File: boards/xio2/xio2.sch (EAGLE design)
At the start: 268 parts, among them J1 12401598E4#2A, Q1 BSS138, Q2 BSS138, X1 MINI-USB-UX60-MB-5ST, Y2 NX3225SA-12.000MHZ-STD-CSR-1

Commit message: More work on the S7. The parallel bus is now alive
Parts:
- added MUX-HI, MUX-LO: IDTQS3VH257, sjg-logic:IDTQS3VH257
- renumbered U$1 to S7
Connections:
- new net HOST_!EXTSEL!: JP1.35, S7-B14.IO_L17P_T2_D30_14@J11
- new net HOST_!HALT!: JP1.37, S7-B14.IO_L17N_T2_D29_14@J12
- new net HOST_!IRQ!: JP1.39, S7-B14.IO_L19P_T3_D26_14@K11
- new net HOST_!MPD!: JP1.32, S7-B14.IO_L19N_T3_D25_VREF_14@K12
- new net HOST_!REF!: JP1.34, S7-B14.IO_L20P_T3_D24_14@M11
- new net HOST_!RST!: JP1.36, S7-B14.IO_L20N_T3_D23_14@M12
- new net HOST_A0: JP1.1, S7-B14.IO_L3P_T0_DQS_PUDC_B_14@B10
- new net HOST_A1: JP1.3, S7-B14.IO_L3N_T0_DQS_EMCCLK_14@A10
- new net HOST_A10: JP1.21, S7-B14.IO_L8N_T1_D12_14@D13
- new net HOST_A11: JP1.23, S7-B14.IO_L9P_T1_DQS_14@G14
- new net HOST_A12: JP1.25, S7-B14.IO_L9N_T1_DQS_D13_14@F14
- new net HOST_A13: JP1.27, S7-B14.IO_L10P_T1_D14_14@F13
- new net HOST_A14: JP1.29, S7-B14.IO_L10N_T1_D15_14@E13
- new net HOST_A15: JP1.31, S7-B14.IO_L11P_T1_SRCC_14@D14
- new net HOST_A2: JP1.5, S7-B14.IO_L4P_T0_D04_14@A12
- new net HOST_A3: JP1.7, S7-B14.IO_L4N_T0_D05_14@A13
- new net HOST_A4: JP1.9, S7-B14.IO_L5P_T0_D06_14@B13
- new net HOST_A5: JP1.11, S7-B14.IO_L5N_T0_D07_14@B14
- new net HOST_A6: JP1.13, S7-B14.IO_L6N_T0_D08_VREF_14@C12
- new net HOST_A7: JP1.15, S7-B14.IO_L7P_T1_D09_14@F12
- new net HOST_A8: JP1.17, S7-B14.IO_L7N_T1_D10_14@E12
- new net HOST_A9: JP1.19, S7-B14.IO_L8P_T1_D11_14@D12
- new net HOST_CLK: JP1.33, S7-B14.IO_0_14@E11
- new net HOST_CTL0: JP1.2, S7-B14.IO_L23P_T3_D19_14@N10
- new net HOST_CTL1: JP1.4, S7-B14.IO_L23N_T3_D18_14@N11
- new net HOST_D0: JP1.6, S7-B14.IO_L11N_T1_SRCC_14@C14
- new net HOST_D1: JP1.8, S7-B14.IO_L12P_T1_MRCC_14@G11
- new net HOST_D2: JP1.10, S7-B14.IO_L12N_T1_MRCC_14@F11
- new net HOST_D3: JP1.12, S7-B14.IO_L13P_T2_MRCC_14@H11
- new net HOST_D4: JP1.14, S7-B14.IO_L13N_T2_MRCC_14@H12
- new net HOST_D5: JP1.16, S7-B14.IO_L15P_T2_DQS_RDWR_B_14@M13
- new net HOST_D6: JP1.18, S7-B14.IO_L16P_T2_CSI_B_14@L12
- new net HOST_D7: JP1.20, S7-B14.IO_L16N_T2_D31_14@L13
- new net HOST_DIR0: JP1.22, S7-B34.IO_0_34@B6
- new net HOST_DIR1: JP1.24, S7-B34.IO_L1P_T0_34@D3
- new net HOST_DIR2: JP1.26, S7-B34.IO_L1N_T0_34@C3
- new net HOST_DIR3: JP1.28, S7-B34.IO_L2P_T0_34@A4
- new net HOST_DIR4: JP1.30, S7-B34.IO_L2N_T0_34@A3
- new net HOST_R/!W!: JP1.38, S7-B14.IO_L1P_T0_D00_MOSI_14@B11
- new net SPI_IRQ: S7-B34.IO_L22N_T3_34@L2
- new net STMDATA_A0: MUX-LO.A0@2, S7-B34.IO_L3P_T0_DQS_34@B3
- new net STMDATA_A1: MUX-LO.A1@5, S7-B34.IO_L3N_T0_DQS_34@A2
- new net STMDATA_A2: MUX-LO.A2@11, S7-B34.IO_L4P_T0_34@B5
- new net STMDATA_A3: MUX-LO.A3@14, S7-B34.IO_L4N_T0_34@A5
- new net STMDATA_A4: MUX-HI.A0@2, S7-B34.IO_L5P_T0_34@B2
- new net STMDATA_A5: MUX-HI.A1@5, S7-B34.IO_L5N_T0_34@B1
- new net STMDATA_A6: MUX-HI.A2@11, S7-B34.IO_L6P_T0_34@C5
- new net STMDATA_A7: MUX-HI.A3@14, S7-B34.IO_L6N_T0_VREF_34@C4
- new net STMDATA_B0: MUX-LO.B0@3, S7-B34.IO_L7P_T1_34@E4
- new net STMDATA_B1: MUX-LO.B1@6, S7-B34.IO_L7N_T1_34@D4
- new net STMDATA_B2: MUX-LO.B2@10, S7-B34.IO_L8P_T1_34@F3
- new net STMDATA_B3: MUX-LO.B3@13, S7-B34.IO_L8N_T1_34@F2
- new net STMDATA_B4: MUX-HI.B0@3, S7-B34.IO_L9P_T1_DQS_34@G1
- new net STMDATA_B5: MUX-HI.B1@6, S7-B34.IO_L9N_T1_DQS_34@F1
- new net STMDATA_B6: MUX-HI.B2@10, S7-B34.IO_L10P_T1_34@E2
- new net STMDATA_B7: MUX-HI.B3@13, S7-B34.IO_L10N_T1_34@D2
- new net STM_MUX_CTL: MUX-HI.S@1, MUX-LO.S@1
- new net STM_MUX_D0: MUX-LO.Y0@4
- new net STM_MUX_D1: MUX-LO.Y1@7
- new net STM_MUX_D2: MUX-LO.Y2@9
- new net STM_MUX_D3: MUX-LO.Y3@12
- new net STM_MUX_D4: MUX-HI.Y0@4
- new net STM_MUX_D5: MUX-HI.Y1@7
- new net STM_MUX_D6: MUX-HI.Y2@9
- new net STM_MUX_D7: MUX-HI.Y3@12
- net +3V3: now also MUX-HI.VCC@16, MUX-LO.VCC@16, S7-B14.VCCO_14@G13, S7-B14.VCCO_14@K13, S7-B14.VCCO_14@N13, S7-B34.VCCO_34@G2, S7-B34.VCCO_34@K2, S7-B34.VCCO_34@N2
- net GND: now also JP1.40, MUX-HI.!E!@15, MUX-HI.GND@8, MUX-LO.!E!@15, MUX-LO.GND@8
- net LX_CLK: now also S7-B34.IO_L12P_T1_MRCC_34@G4
- net SPI_IRQ0: now also S7-B34.IO_25_34@L5
- net SPI_IRQ1: now also S7-B34.IO_L24N_T3_34@N4
- net SPI_IRQ2: now also S7-B34.IO_L24P_T3_34@P5
- net SPI_IRQ3: now also S7-B34.IO_L23N_T3_34@M4
- net SPI_IRQ4: now also S7-B34.IO_L23P_T3_34@M5
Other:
- note added: "HBus needs rework"
- note added: "STMDATA_A* is an input STMDATA_B* is an output STM controls whether to read or write data using STM_MUX_CTL in IRQ handler"

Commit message: Work in the new configuration for the STM32H743
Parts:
- removed R73, R75, R76, R77: 33R, rcl:R-EU_R0201
- renumbered XIO to U$1
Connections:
- removed net N$73: R76.1, U$1-XSPI.PB4@B7
- removed net N$74: R77.1, U$1-XSPI.PF7@K3
- removed net N$75: R73.1, U$1-XSPI.PA6@R3
- removed net N$76: R91.1, U$1-XSPI.PF9@L4
- removed net XSPI_1_MISO: R73.2
- removed net XSPI_2_MISO: R75.2
- removed net XSPI_2_MOSI: U$1-XSPI.PB15@T15
- removed net XSPI_2_SCK: U$1-XSPI.PB13@U14
- removed net XSPI_3_MISO: R76.2
- removed net XSPI_3_MOSI: U$1-XSPI.PB5@A5
- removed net XSPI_3_SCK: U$1-XSPI.PB3@C6
- net ARCH0: now also U$1-CFG.PC4@T4; no longer U$1-CFG.PG2@H16
- net ARCH1: now also U$1-CFG.PC5@U4; no longer U$1-CFG.PG3@H15
- net ARCH2: now also U$1-CFG.PC14@C2; no longer U$1-CFG.PG6@G15
- net ARCH3: now also U$1-CFG.PC15@C1; no longer U$1-CFG.PG7@F16
- net HOST_A0: now also U$1-HOST.PB0@U5
- net HOST_A1: now also U$1-HOST.PB1@T5
- net HOST_A10: now also U$1-HOST.PB10@P11
- net HOST_A11: now also U$1-HOST.PB11@P12
- net HOST_A12: now also U$1-HOST.PB12@T14
- net HOST_A13: now also U$1-HOST.PB13@U14
- net HOST_A14: now also U$1-HOST.PB15@U15
- net HOST_A15: now also U$1-HOST.PB16@T15
- net HOST_A2: now also U$1-HOST.PB2@R6
- net HOST_A3: now also U$1-HOST.PB3@C6
- net HOST_A4: now also U$1-HOST.PB4@B7
- net HOST_A5: now also U$1-HOST.PB5@A5
- net HOST_A6: now also U$1-HOST.PB6@B5
- net HOST_A7: now also U$1-HOST.PB7@C5
- net HOST_A8: now also U$1-HOST.PB8@D5
- net HOST_A9: now also U$1-HOST.PB9@D4
- net MEM0: now also U$1-CFG.PE3@D3; no longer U$1-CFG.PG10@A9
- net MEM1: now also U$1-CFG.PE4@D2; no longer U$1-CFG.PG11@B9
- net N$13: now also U$1-LED.PD11@R15; no longer U$1-LED.PC13@E3
- net N$14: now also U$1-LED.PD12@R16; no longer U$1-LED.PC14@C2
- net N$15: now also U$1-LED.PD13@R17; no longer U$1-LED.PC15@C1
- net N$72: now also R91.1, U$1-XSPI.PF8@K4; no longer R75.1, U$1-XSPI.PB14@U15
- net SDCD: now also U$1-SDCARD.PC13@E3; no longer U$1-SDCARD.PC7@F13
- net SPI_IRQ0: now also U$1-SPI.PG6@G15; no longer U$1-SPI.PC0@L2
- net SPI_IRQ1: now also U$1-SPI.PG7@F16; no longer U$1-SPI.PC1@M2
- net SPI_IRQ2: now also U$1-SPI.PG9@A10; no longer U$1-SPI.PC2@M3
- net SPI_IRQ3: now also U$1-SPI.PG10@A9; no longer U$1-SPI.PC3@M4
- net SPI_IRQ4: now also U$1-SPI.PG11@B9; no longer U$1-SPI.PC4@T4
- net STM_MUX_CTL: now also U$1-HOST.PC3@M4
- net STM_MUX_D0: now also U$1-HOST.PA0@N5
- net STM_MUX_D1: now also U$1-HOST.PA1@N4
- net STM_MUX_D2: now also U$1-HOST.PA2@N3
- net STM_MUX_D3: now also U$1-HOST.PA3@U2
- net STM_MUX_D4: now also U$1-HOST.PA4@U3
- net STM_MUX_D5: now also U$1-HOST.PA5@T3
- net STM_MUX_D6: now also U$1-HOST.PA6@R3
- net STM_MUX_D7: now also U$1-HOST.PA7@R5
- net XIO_RX: now also U$1-POWER.PC7@F13; no longer U$1-POWER.PA1@N4
- net XIO_TX: now also U$1-POWER.PC6@F14; no longer U$1-POWER.PA0@N5
- net XSPI_1_MOSI: no longer U$1-XSPI.PA7@R5
- net XSPI_1_SCK: no longer U$1-XSPI.PA5@T3
- net XSPI_5_MISO: now also R91.2; no longer U$1-XSPI.PF8@K4
- net XSPI_5_MOSI: now also U$1-XSPI.PF9@L4; no longer R91.2
- net XSPI_5_SCK: now also U$1-XSPI.PF7@K3; no longer R77.2
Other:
- note added: "FPGA SPI, @ 100MHz"
- note added: "FPGA to STM32 Host interface"
- note added: "SPI5 to be used with FPGA as master. SPI6 to be used with STM as master Resistors sited close to source signal"
- note added: "Slot SPI, @ 100MHz"
- note removed: "SPI1, SPI2, SPI3 to be used with FPGA as master. SPI5, SPI6 to be used with STM as master Resistors sited close to source signal"
- note removed: "Slot SPI, runs at up to 45MHz"
- moved on the sheet: R26, R27, R91, R92, R93

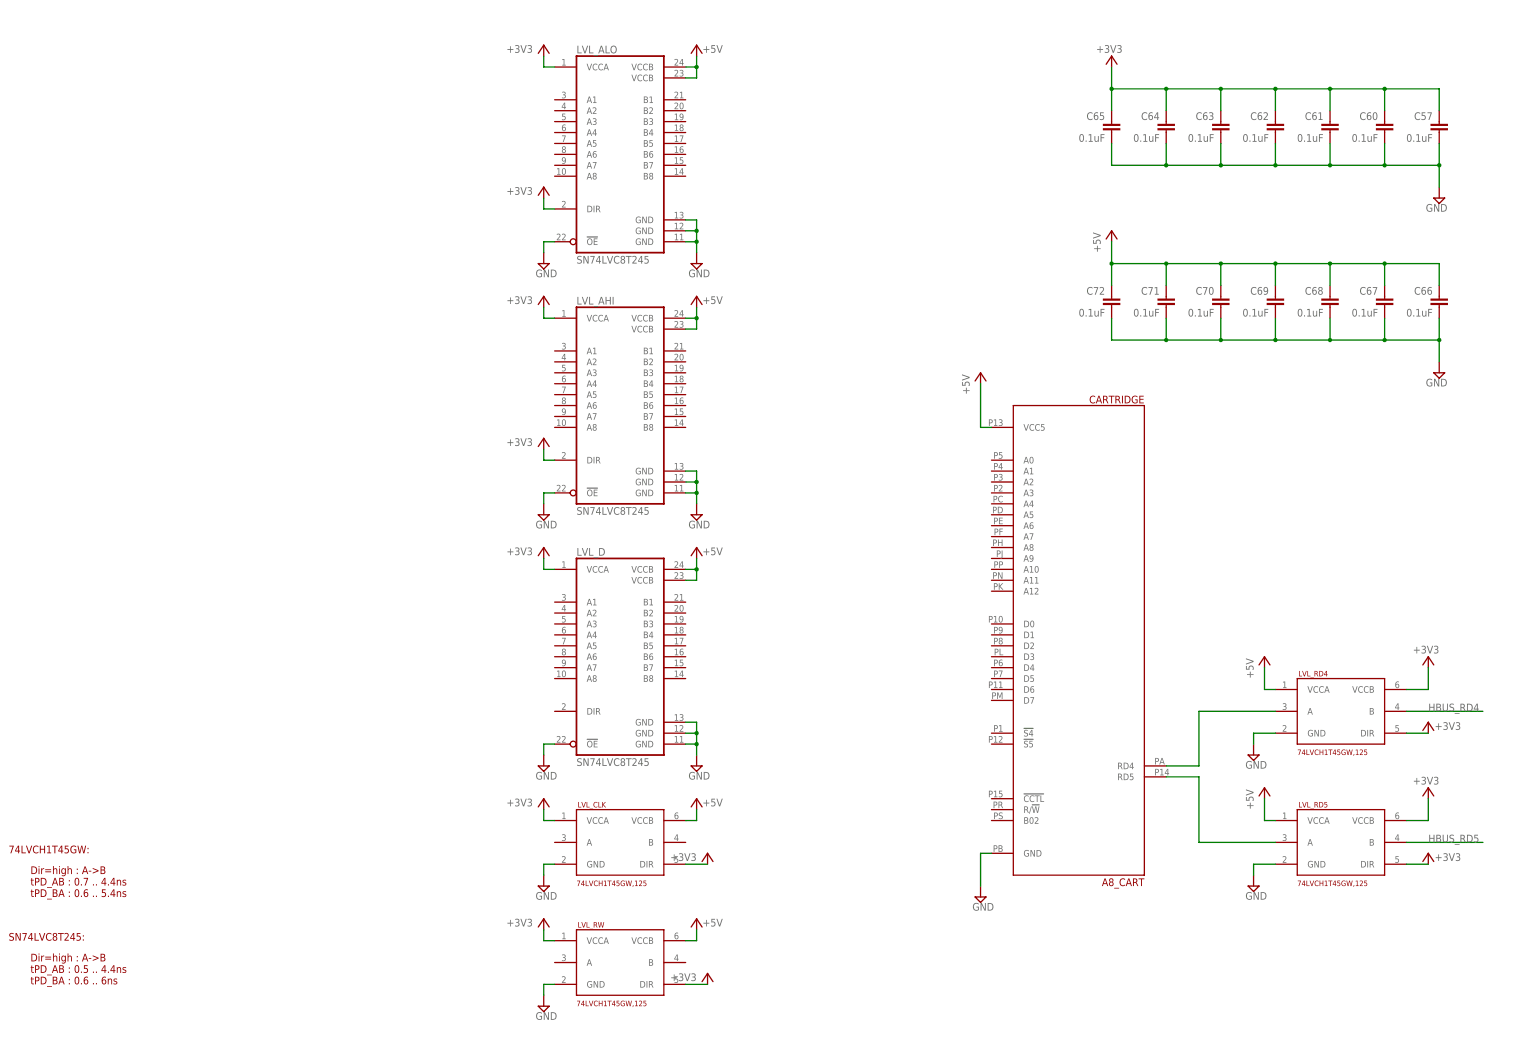
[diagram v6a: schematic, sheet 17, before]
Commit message: Update to a “working board” scenario. Need to cross-check everything, and start to work on layout
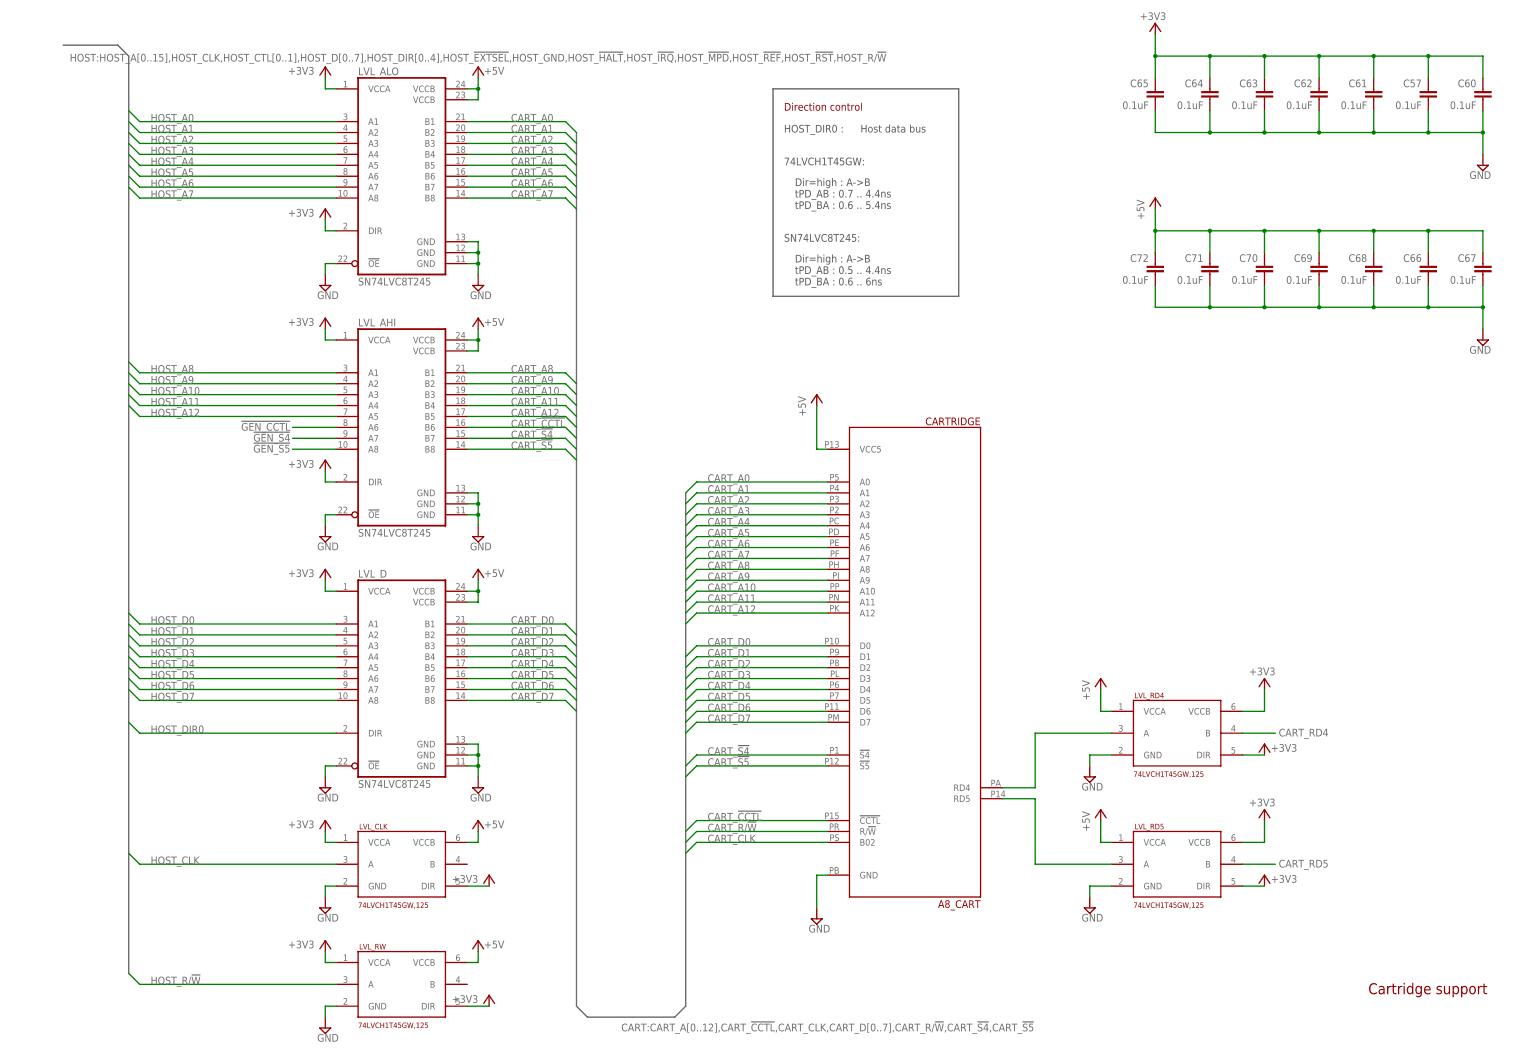
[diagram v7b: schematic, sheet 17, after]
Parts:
- removed R80: 33R, rcl:R-EU_R0402
- added C100, C88: 0.1uF, rcl:C-EUC0201
- added R73, R75: 33R, rcl:R-EU_R0201
- C101, C52, C73, C77: device rcl:C-EUC1210 -> rcl:C-EUC0805
- C102, C59, C74, C75, C76, C78, C79, C82: device rcl:C-EUC0805 -> rcl:C-EUC0402
- C104, C30, C36, C47, C48, C49, C50, C51, C58, C83, C84, C85, C86: device rcl:C-EUC0603 -> rcl:C-EUC0201
- C134, C135, C136, C137, C167, C168, C169, C170, C171, C172, C173, C174, C175, C177, C19, C20, C21, C22, C23, C24, C25, C35, C53, C54, C55, C56, C57, C60, C61, C62, C63, C64, C65, C66, C67, C68, C69, C70, C71, C72, C81, C95, C96, C97, C98: device rcl:C-EUC0402K -> rcl:C-EUC0201
- R14, R15, R16, R17, R18, R2, R3, R36, R37, R38, R39, R4, R40, R41, R50, R51, R52, R54, R55, R56, R57, R58, R59, R6, R60, R61, R62, R63, R64, R65, R66, R67, R68, R69, R7, R70, R71, R74, R78, R79, R8, R83, R84, R85, R88, R89, R9, R90: device rcl:R-EU_R0402 -> rcl:R-EU_R0201
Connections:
- removed net XSPI_1_MOSI: R74.2
- removed net XSPI_1_SCK: R80.2
- new net !ADDR_VALID_READ!: S7-B34.IO_L11P_T1_SRCC_34@D1
- new net !ADDR_VALID_WRITE!: S7-B34.IO_L11N_T1_SRCC_34@C1
- new net !GEN_CCTL!: LVL_AHI.A6@8, S7-B34.IO_L12N_T1_MRCC_34@F4
- new net !GEN_S4!: LVL_AHI.A7@9, S7-B34.IO_L13N_T2_MRCC_34@H3
- new net !GEN_S5!: LVL_AHI.A8@10, S7-B34.IO_L14P_T2_SRCC_34@H2
- new net CART_!CCTL!: CARTRIDGE.!CCTL!@15, LVL_AHI.B6@16
- new net CART_!S4!: CARTRIDGE.!S4!@1, LVL_AHI.B7@15
- new net CART_!S5!: CARTRIDGE.!S5!@12, LVL_AHI.B8@14
- new net CART_A0: CARTRIDGE.A0@5, LVL_ALO.B1@21
- new net CART_A1: CARTRIDGE.A1@4, LVL_ALO.B2@20
- new net CART_A10: CARTRIDGE.A10@P, LVL_AHI.B3@19
- new net CART_A11: CARTRIDGE.A11@N, LVL_AHI.B4@18
- new net CART_A12: CARTRIDGE.A12@K, LVL_AHI.B5@17
- new net CART_A2: CARTRIDGE.A2@3, LVL_ALO.B3@19
- new net CART_A3: CARTRIDGE.A3@2, LVL_ALO.B4@18
- new net CART_A4: CARTRIDGE.A4@C, LVL_ALO.B5@17
- new net CART_A5: CARTRIDGE.A5@D, LVL_ALO.B6@16
- new net CART_A6: CARTRIDGE.A6@E, LVL_ALO.B7@15
- new net CART_A7: CARTRIDGE.A7@F, LVL_ALO.B8@14
- new net CART_A8: CARTRIDGE.A8@H, LVL_AHI.B1@21
- new net CART_A9: CARTRIDGE.A9@J, LVL_AHI.B2@20
- new net CART_CLK: CARTRIDGE.B02@S
- new net CART_D0: CARTRIDGE.D0@10, LVL_D.B1@21
- new net CART_D1: CARTRIDGE.D1@9, LVL_D.B2@20
- new net CART_D2: CARTRIDGE.D2@8, LVL_D.B3@19
- new net CART_D3: CARTRIDGE.D3@L, LVL_D.B4@18
- new net CART_D4: CARTRIDGE.D4@6, LVL_D.B5@17
- new net CART_D5: CARTRIDGE.D5@7, LVL_D.B6@16
- new net CART_D6: CARTRIDGE.D6@11, LVL_D.B7@15
- new net CART_D7: CARTRIDGE.D7@M, LVL_D.B8@14
- new net CART_R/!W!: CARTRIDGE.R/!W!@R
- new net CART_RD4: LVL_RD4.B@4, S7-B34.IO_L14N_T2_SRCC_34@H1
- new net CART_RD5: LVL_RD5.B@4, S7-B34.IO_L15P_T2_DQS_34@J2
- new net N$73: R74.2, S7-B34.IO_L22P_T3_34@L3
- new net N$74: R75.2, S7-B34.IO_L21P_T3_DQS_34@P4
- new net N$75: R73.2, S7-B34.IO_L20P_T3_34@P2
- new net XPSI5_MOSI: R74.1
- new net XSPI5_MISO: S7-B34.IO_L21N_T3_DQS_34@P3
- new net XSPI5_SCK: R75.1
- new net XSPI6_MISO: R73.1
- new net XSPI6_MOSI: S7-B34.IO_L20N_T3_34@N1
- new net XSPI6_SCK: S7-B34.IO_L19N_T3_VREF_34@M2
- net +3V3: now also C100.1, C88.1
- net GND: now also C100.2, C88.2
- net HBUS_RD4: no longer LVL_RD4.B@4
- net HBUS_RD5: no longer LVL_RD5.B@4
- net HOST_A0: now also LVL_ALO.A1@3
- net HOST_A1: now also LVL_ALO.A2@4
- net HOST_A10: now also LVL_AHI.A3@5
- net HOST_A11: now also LVL_AHI.A4@6
- net HOST_A12: now also LVL_AHI.A5@7
- net HOST_A2: now also LVL_ALO.A3@5
- net HOST_A3: now also LVL_ALO.A4@6
- net HOST_A4: now also LVL_ALO.A5@7
- net HOST_A5: now also LVL_ALO.A6@8
- net HOST_A6: now also LVL_ALO.A7@9
- net HOST_A7: now also LVL_ALO.A8@10
- net HOST_A8: now also LVL_AHI.A1@3
- net HOST_A9: now also LVL_AHI.A2@4
- net HOST_CLK: now also LVL_CLK.A@3
- net HOST_D0: now also LVL_D.A1@3
- net HOST_D1: now also LVL_D.A2@4
- net HOST_D2: now also LVL_D.A3@5
- net HOST_D3: now also LVL_D.A4@6
- net HOST_D4: now also LVL_D.A5@7
- net HOST_D5: now also LVL_D.A6@8
- net HOST_D6: now also LVL_D.A7@9
- net HOST_D7: now also LVL_D.A8@10
- net HOST_DIR0: now also LVL_D.DIR@2
- net HOST_R/!W!: now also LVL_RW.A@3
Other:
- note added: "100uF caps can be placed anywhere others within 2 electrical inches of part"
- note added: ": GRM21BR60J107ME15L (0805) : GRM21BR60J476ME15L (0805) : GRM155R60J475ME87D (0402) : GRM033R60J474KE90D (0201)"
- note added: "Bypass caps for muxes"
- note added: "Cartridge"
- note added: "Cartridge support"
- note added: "Direction control"
- note added: "FPGA Bank 14"
- note added: "FPGA Bank 34"
- note added: "HOST_DIR0 :"
- note added: "HOST_DIR0 : HOST_DIR1 : HOST_DIR2 : HOST_DIR3 : HOST_DIR4 :"
- note added: "Host data bus"
- note added: "Host data bus Host address bus Host R/!W! signal Host !REF! signal Host !HALT! signal"
- note added: "SPI termination"
- note added: "SPI5 @ 100 MHz"
- note added: "SPI6 @ 100MHz"
- note added: "STM32 data bus"
- note added: "STMDATA_A* is an input STMDATA_B* is an output STM controls whether to read or write data using STM_MUX_CTL in IRQ handler Mux removes need to sync FPGA & STM"
- note removed: "1210 caps can be placed anywhere 0805 caps within 2 electrical inches of part 0603 caps within 2 electrical inches of part"
- note removed: ": GRM32ER60J107ME20L : GRM32ER70J476ME20L : GRM21BR71A475KA73 : GRM188R70J474KA01"
- note removed: "FPGA Clock, Banks 0 & 1"
- note removed: "SPI1 @ 150 MHz"
- note removed: "SPI2 @ 100MHz"
- note removed: "STMDATA_A* is an input STMDATA_B* is an output STM controls whether to read or write data using STM_MUX_CTL in IRQ handler"
- moved on the sheet: C35, C57, C60, C61, C62, C63, C64, C65, C66, C67, C68, C69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
